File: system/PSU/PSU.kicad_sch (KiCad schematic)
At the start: 21 parts, among them IC2 LM723, M2 -15V METER, P2 2k5, T2 2N3055

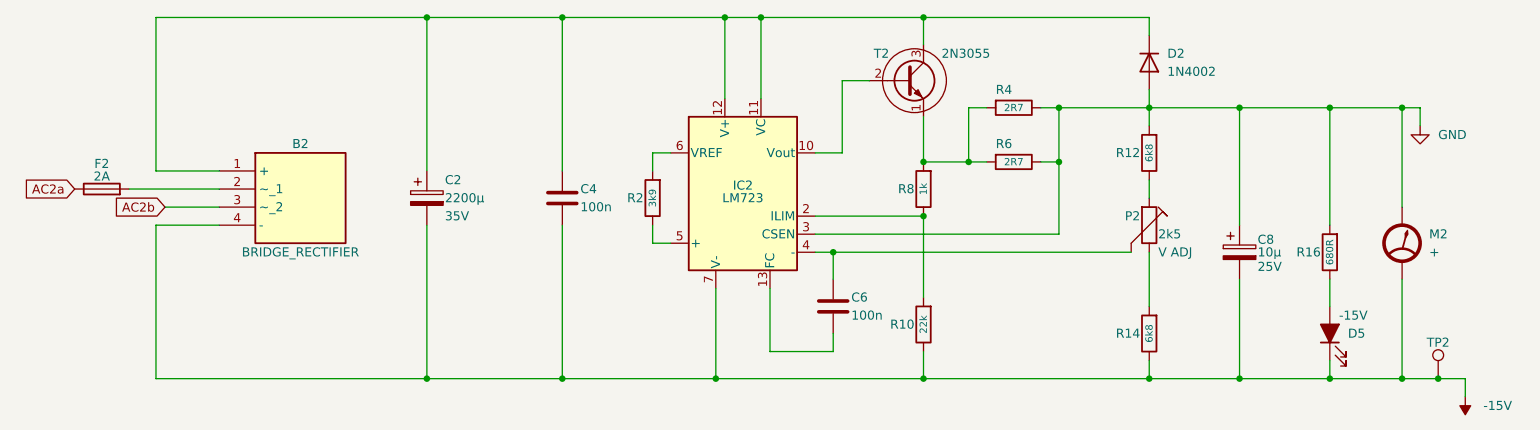
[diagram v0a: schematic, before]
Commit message: fixed PSU values; reorganized PSU info
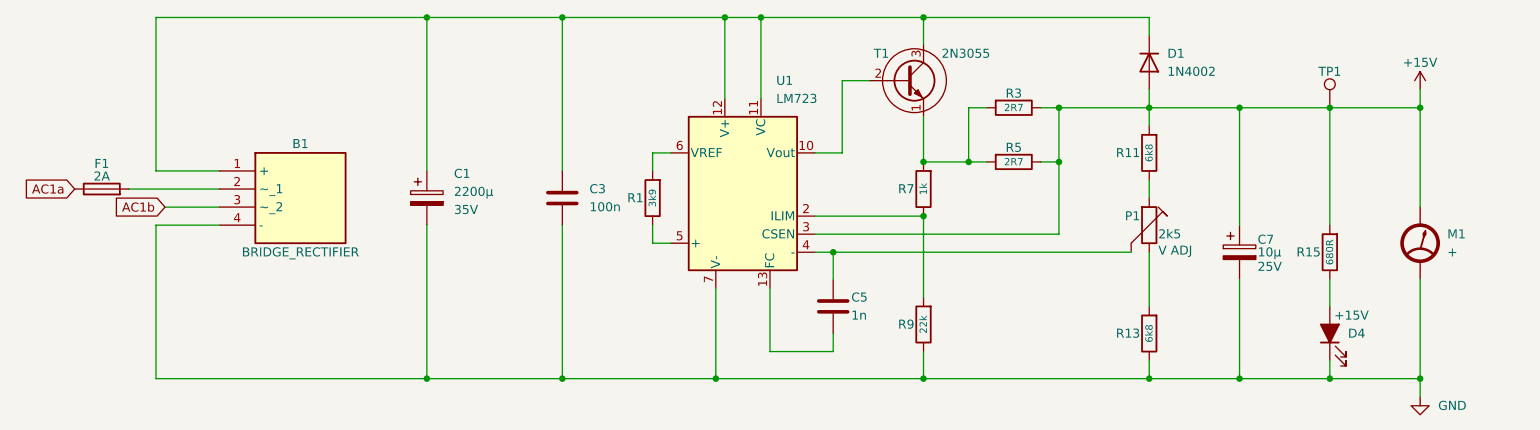
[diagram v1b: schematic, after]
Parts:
- removed B2: BRIDGE_RECTIFIER, FormantKO:BridgeRectifier, symbol FormantKO:BridgeRectifier
- removed C2: 2200µ, Capacitor_THT:CP_Axial_L42.0mm_D23.0mm_P45.00mm_Horizontal, symbol FormantKO:C_Polarized
- removed C4, C6: 100n, FormantKO:C_Rect_300, symbol FormantKO:C
- removed C8: 10µ, Capacitor_THT:CP_Radial_Tantal_D4.5mm_P5.00mm, symbol FormantKO:C_Polarized
- removed D2: 1N4002, Diode_THT:D_DO-41_SOD81_P12.70mm_Horizontal, symbol Diode:1N4002
- removed D5: -15V LED, FormantKO:PanelConnector_1x02, symbol FormantKO:D_LED
- removed F2: 2A, FormantKO:FuseHolder_5x20mm, symbol FormantKO:Fuse
- removed IC2: LM723, FormantKO:DIP-14, symbol FormantKO:LM723
- removed M2: -15V METER, FormantKO:PanelConnector_1x02, symbol FormantKO:Meter
- removed P2: 2k5, FormantKO:Potentiometer_Trimmer_MultiTurn, symbol FormantKO:R_Trim_MultiTurn
- removed R10: 22k, FormantKO:R_Axial_Horizontal, symbol FormantKO:R
- removed R12, R14: 6k8, FormantKO:R_Axial_Horizontal, symbol FormantKO:R
- removed R16: 680R, FormantKO:R_Axial_Horizontal, symbol FormantKO:R
- removed R2: 3k9, FormantKO:R_Axial_Horizontal, symbol FormantKO:R
- removed R4, R6: 2R7, FormantKO:R_Axial_Horizontal, symbol FormantKO:R
- removed R8: 1k, FormantKO:R_Axial_Horizontal, symbol FormantKO:R
- removed T2: 2N3055, FormantKO:PowerTransistorConnector_EBC, symbol FormantKO:2N3055
- removed TP2: -15V, TestPoint:TestPoint_Loop_D1.80mm_Drill1.0mm_Beaded, symbol Connector:TestPoint
- added B1: BRIDGE_RECTIFIER, FormantKO:BridgeRectifier, symbol FormantKO:BridgeRectifier
- added C1: 2200µ, Capacitor_THT:CP_Axial_L42.0mm_D23.0mm_P45.00mm_Horizontal, symbol FormantKO:C_Polarized
- added C3: 100n, FormantKO:C_Rect_300, symbol FormantKO:C
- added C5: 1n, FormantKO:C_Rect_300, symbol FormantKO:C
- added C7: 10µ, Capacitor_THT:CP_Radial_Tantal_D4.5mm_P5.00mm, symbol FormantKO:C_Polarized
- added D1: 1N4002, Diode_THT:D_DO-41_SOD81_P12.70mm_Horizontal, symbol Diode:1N4002
- added D4: +15V LED, FormantKO:PanelConnector_1x02, symbol FormantKO:D_LED
- added F1: 2A, FormantKO:FuseHolder_5x20mm, symbol FormantKO:Fuse
- added M1: +15V METER, FormantKO:PanelConnector_1x02, symbol FormantKO:Meter
- added P1: 2k5, FormantKO:Potentiometer_Trimmer_MultiTurn, symbol FormantKO:R_Trim_MultiTurn
- added R1: 3k9, FormantKO:R_Axial_Horizontal, symbol FormantKO:R
- added R11, R13: 6k8, FormantKO:R_Axial_Horizontal, symbol FormantKO:R
- added R15: 680R, FormantKO:R_Axial_Horizontal, symbol FormantKO:R
- added R3, R5: 2R7, FormantKO:R_Axial_Horizontal, symbol FormantKO:R
- added R7: 1k, FormantKO:R_Axial_Horizontal, symbol FormantKO:R
- added R9: 22k, FormantKO:R_Axial_Horizontal, symbol FormantKO:R
- added T1: 2N3055, FormantKO:PowerTransistorConnector_EBC, symbol FormantKO:2N3055
- added TP1: +15V, TestPoint:TestPoint_Loop_D1.80mm_Drill1.0mm_Beaded, symbol Connector:TestPoint
- added U1: LM723, FormantKO:DIP-14, symbol FormantKO:LM723
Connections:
- net GND: now also B1.4 (-), C1.2, C3.1, C7.2, D4.1 (K), M1.1 (-), R13.1, R9.1, U1.7 (V-)
- new net: R3.2, R5.2, R7.2, T1.1 (E)
- new net: B1.1 (+), C1.1, C3.2, D1.1 (K), T1.3 (C), U1.11 (VC), U1.12 (V+)
- new net: D4.2 (A), R15.1
- new net: R1.1, U1.5 (+)
- new net: R1.2, U1.6 (VREF)
- new net: P1.1, R13.2
- new net: C5.1, U1.13 (FC)
- new net: C5.2, P1.2, U1.4 (-)
- new net: T1.2 (B), U1.10 (Vout)
- new net: R7.1, R9.2, U1.2 (ILIM)
- new net: B1.2 (~_1), F1.2
- new net: P1.3, R11.1
- new net +15V: C7.1, D1.2 (A), M1.2 (+), R11.2, R15.2, R3.1, R5.1, TP1.1, U1.3 (CSEN)
- new net AC1a: F1.1
- new net AC1b: B1.3 (~_2)

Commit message: com revamp
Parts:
- D1: footprint Diode_THT:D_DO-41_SOD81_P12.70mm_Horizontal -> FormantKO:DO-41; symbol Diode:1N4002 -> FormantKO:1N4002
- M1: Legend (none) -> +15V METER
- TP1: footprint TestPoint:TestPoint_Loop_D1.80mm_Drill1.0mm_Beaded -> FormantKO:KEYSTONE_5001; symbol Connector:TestPoint -> FormantKO:TestPoint
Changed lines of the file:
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@@
 	)
 	(symbol
-		(lib_id "Diode:1N4002")
+		(lib_id "FormantKO:1N4002")
 		(at 203.2 82.55 270)
 		(unit 1)
@@
 			)
 		)
-		(property "Footprint" "Diode_THT:D_DO-41_SOD81_P12.70mm_Horizontal"
-			(at 198.755 82.55 0)
+		(property "Footprint" "FormantKO:DO-41"
+			(at 203.2 82.55 0)
 			(hide yes)
 			(show_name no)
@@
 			)
 		)
-		(property "Description" "100V 1A General Purpose Rectifier Diode, DO-41"
+		(property "Description" "50V 1A General Purpose Rectifier Diode, DO-41"
 			(at 203.2 82.55 0)
 			(hide yes)
@@
 	)
 	(symbol
-		(lib_id "Connector:TestPoint")
+		(lib_id "FormantKO:TestPoint")
 		(at 228.6 88.9 0)
 		(unit 1)
@@
 		(dnp no)
 		(property "Reference" "TP1"
-			(at 228.6 83.82 0)
-			(show_name no)
-			(do_not_autoplace no)
-			(effects
-				(font
-					(size 1.27 1.27)
-				)
+			(at 228.6 87.63 0)
+			(show_name no)
+			(do_not_autoplace no)
+			(effects
+				(font
+					(size 1.27 1.27)
+				)
+				(justify bottom)
 			)
 		)
@@
 			)
 		)
-		(property "Footprint" "TestPoint:TestPoint_Loop_D1.80mm_Drill1.0mm_Beaded"
+		(property "Footprint" "FormantKO:KEYSTONE_5001"
 			(at 233.68 88.9 0)
 			(hide yes)
@@
 			(hide yes)
 			(show_name no)
+			(do_not_autoplace no)
+			(effects
+				(font
+					(size 1.27 1.27)
+				)
+			)
+		)
+		(property "Legend" "+15V METER"
+			(at 241.3 107.95 0)
+			(hide yes)
+			(show_name no)
